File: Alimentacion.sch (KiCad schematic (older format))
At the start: 5 parts, among them CON1 BARREL_JACK, U4 LM7805CT

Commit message: finalizado enrutado provisional
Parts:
- D1: footprint Diodes_ThroughHole:Diode_DO-35_SOD27_Horizontal_RM10 -> Diodos:DO-214AC
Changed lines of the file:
@@
 $Descr A4 11693 8268
 encoding utf-8
-Sheet 3 14
+Sheet 2 15
 Title ""
 Date ""
@@
 F 0 "D1" H 4950 2700 50  0000 C CNN
 F 1 "1N4002" H 4950 2500 50  0000 C CNN
-F 2 "Diodes_ThroughHole:Diode_DO-35_SOD27_Horizontal_RM10" H 4950 2600 50  0001 C CNN
+F 2 "Diodos:DO-214AC" H 4950 2600 50  0001 C CNN
 F 3 "" H 4950 2600 50  0000 C CNN
 F 4 "DC COMPONENTS" H 4950 2600 60  0001 C CNN "Fabricante"
@@
 Alimentador de corriente\nTME AK-TB-02\nFabricante AKYGA\nRef: CPSUNOTAKY-07290
 $Comp
-L +5V #PWR08
+L +5V #PWR01
 U 1 1 5793C6D2
 P 7050 2450
-F 0 "#PWR08" H 7050 2300 50  0001 C CNN
+F 0 "#PWR01" H 7050 2300 50  0001 C CNN
 F 1 "+5V" H 7050 2590 50  0000 C CNN
 F 2 "" H 7050 2450 50  0000 C CNN
@@
 $EndComp
 $Comp
-L GND #PWR09
+L GND #PWR02
 U 1 1 5793C6D8
 P 6050 3350
-F 0 "#PWR09" H 6050 3100 50  0001 C CNN
+F 0 "#PWR02" H 6050 3100 50  0001 C CNN
 F 1 "GND" H 6050 3200 50  0000 C CNN
 F 2 "" H 6050 3350 50  0000 C CNN
@@
 $EndComp
 $Comp
-L PWR_FLAG #FLG010
+L PWR_FLAG #FLG03
 U 1 1 5793C6DE
 P 4650 2450
-F 0 "#FLG010" H 4650 2545 50  0001 C CNN
+F 0 "#FLG03" H 4650 2545 50  0001 C CNN
 F 1 "PWR_FLAG" H 4650 2630 50  0000 C CNN
 F 2 "" H 4650 2450 50  0000 C CNN
@@
 $EndComp
 $Comp
-L PWR_FLAG #FLG011
+L PWR_FLAG #FLG04
 U 1 1 5793C6E4
 P 4950 3100
-F 0 "#FLG011" H 4950 3195 50  0001 C CNN
+F 0 "#FLG04" H 4950 3195 50  0001 C CNN
 F 1 "PWR_FLAG" H 4950 3280 50  0000 C CNN
 F 2 "" H 4950 3100 50  0000 C CNN
@@
 $EndComp
 $Comp
-L VCC #PWR012
+L VCC #PWR05
 U 1 1 5793C6EA
 P 7300 2450
-F 0 "#PWR012" H 7300 2300 50  0001 C CNN
+F 0 "#PWR05" H 7300 2300 50  0001 C CNN
 F 1 "VCC" H 7300 2600 50  0000 C CNN
 F 2 "" H 7300 2450 50  0000 C CNN

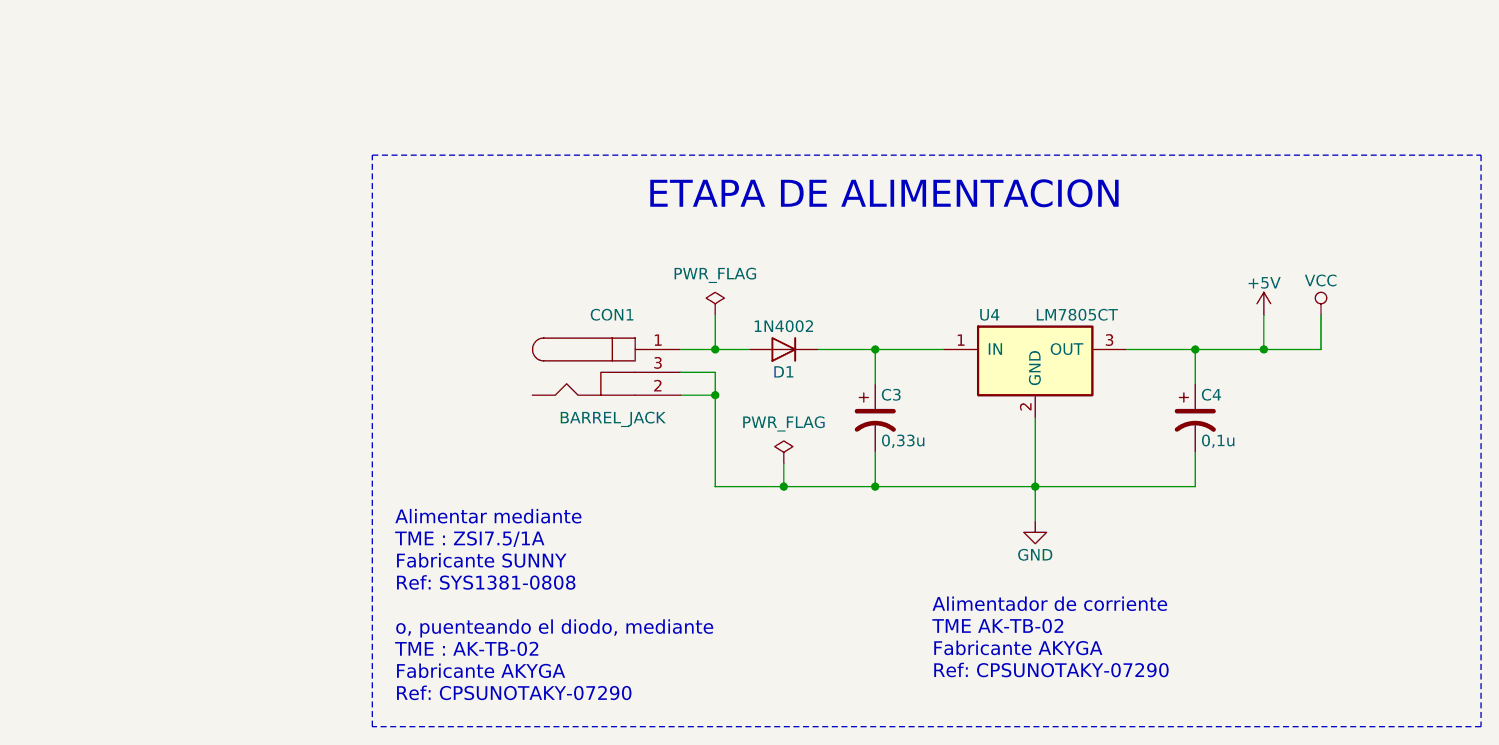
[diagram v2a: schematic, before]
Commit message: añadiendo valores del distribuidor a los componentes
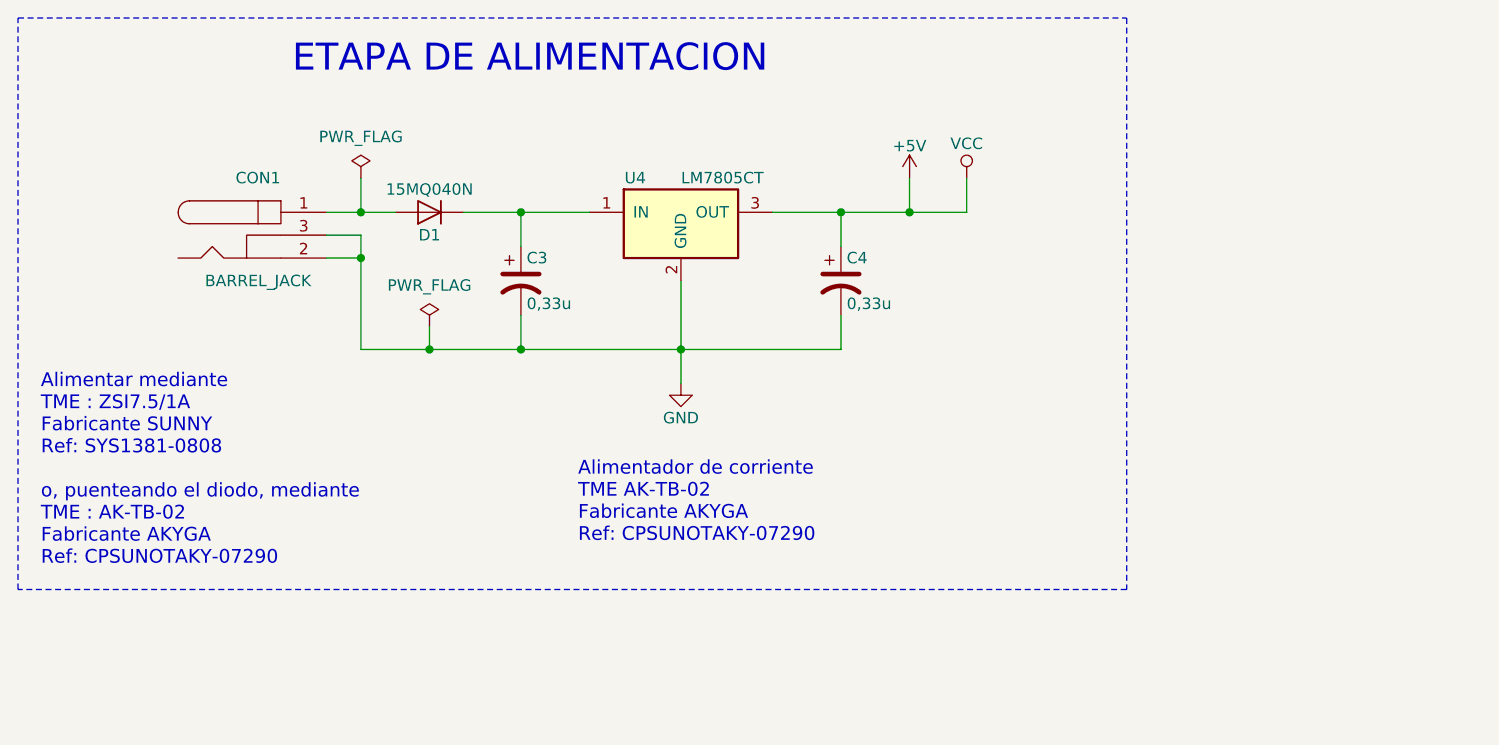
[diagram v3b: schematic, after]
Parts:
- C3: Ref UMT1HR33MDD -> UVZ1H330MDD; Ref_Proveedor UMT1HR33MDD -> UVZ1H330MDD
- C4: value 0,1u -> 0,33u; Ref UMT1H0R1MDD -> UVZ1H330MDD; Ref_Proveedor UMT1H0R1MDD -> UVZ1H330MDD
- D1: value 1N4002 -> 15MQ040N; Fabricante DC COMPONENTS -> VISHAY; Ref 1N4002 -> 15MQ040N; Ref_Proveedor 1N4002-DC -> 15MQ040NTRPBF
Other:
- moved on the sheet: C3, C4, CON1, D1, U4

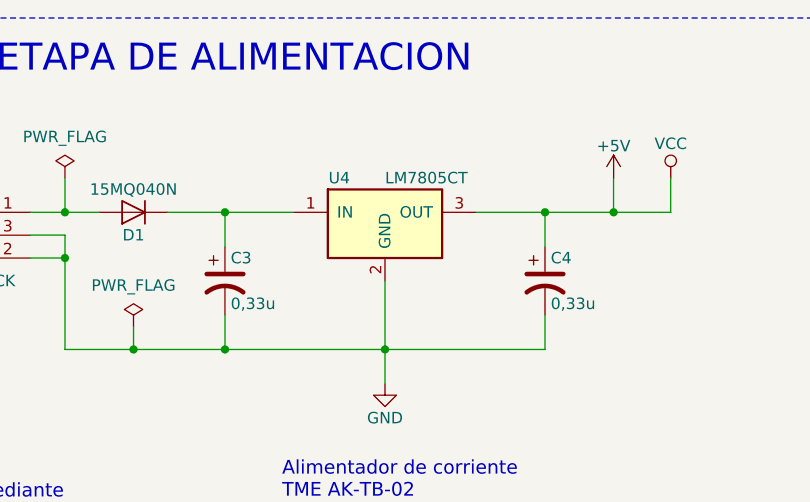
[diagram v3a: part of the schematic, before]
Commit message: ordenar referencias de componentes
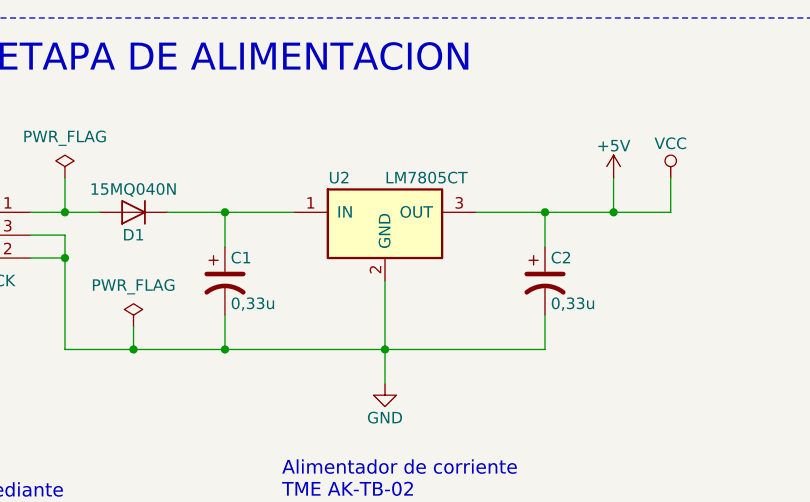
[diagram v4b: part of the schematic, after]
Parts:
- renumbered C3 to C1, C4 to C2, U4 to U2
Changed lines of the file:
@@
 $Descr User 8268 5846
 encoding utf-8
-Sheet 2 15
+Sheet 3 15
 Title ""
 Date ""
@@
 $EndComp
 $Comp
-L CP1 C3
+L CP1 C1
 U 1 1 5793C6BD
 P 3800 2300
-F 0 "C3" H 3825 2400 50  0000 L CNN
+F 0 "C1" H 3825 2400 50  0000 L CNN
 F 1 "0,33u" H 3825 2200 50  0000 L CNN
 F 2 "Capacitors_ThroughHole:C_Radial_D5_L11_P2" H 3800 2300 50  0001 C CNN
@@
 $EndComp
 $Comp
-L CP1 C4
+L CP1 C2
 U 1 1 5793C6CA
 P 5200 2300
-F 0 "C4" H 5225 2400 50  0000 L CNN
+F 0 "C2" H 5225 2400 50  0000 L CNN
 F 1 "0,33u" H 5225 2200 50  0000 L CNN
 F 2 "Capacitors_ThroughHole:C_Radial_D5_L11_P2" H 5200 2300 50  0001 C CNN
@@
 Alimentador de corriente\nTME AK-TB-02\nFabricante AKYGA\nRef: CPSUNOTAKY-07290
 $Comp
-L +5V #PWR01
+L +5V #PWR6
 U 1 1 5793C6D2
 P 5500 1850
-F 0 "#PWR01" H 5500 1700 50  0001 C CNN
+F 0 "#PWR6" H 5500 1700 50  0001 C CNN
 F 1 "+5V" H 5500 1990 50  0000 C CNN
 F 2 "" H 5500 1850 50  0000 C CNN
@@
 $EndComp
 $Comp
-L GND #PWR02
+L GND #PWR5
 U 1 1 5793C6D8
 P 4500 2750
-F 0 "#PWR02" H 4500 2500 50  0001 C CNN
+F 0 "#PWR5" H 4500 2500 50  0001 C CNN
 F 1 "GND" H 4500 2600 50  0000 C CNN
 F 2 "" H 4500 2750 50  0000 C CNN
@@
 $EndComp
 $Comp
-L PWR_FLAG #FLG03
+L PWR_FLAG #FLG1
 U 1 1 5793C6DE
 P 3100 1850
-F 0 "#FLG03" H 3100 1945 50  0001 C CNN
+F 0 "#FLG1" H 3100 1945 50  0001 C CNN
 F 1 "PWR_FLAG" H 3100 2030 50  0000 C CNN
 F 2 "" H 3100 1850 50  0000 C CNN
@@
 $EndComp
 $Comp
-L PWR_FLAG #FLG04
+L PWR_FLAG #FLG2
 U 1 1 5793C6E4
 P 3400 2500
-F 0 "#FLG04" H 3400 2595 50  0001 C CNN
+F 0 "#FLG2" H 3400 2595 50  0001 C CNN
 F 1 "PWR_FLAG" H 3400 2680 50  0000 C CNN
 F 2 "" H 3400 2500 50  0000 C CNN
@@
 $EndComp
 $Comp
-L VCC #PWR05
+L VCC #PWR7
 U 1 1 5793C6EA
 P 5750 1850
-F 0 "#PWR05" H 5750 1700 50  0001 C CNN
+F 0 "#PWR7" H 5750 1700 50  0001 C CNN
 F 1 "VCC" H 5750 2000 50  0000 C CNN
 F 2 "" H 5750 1850 50  0000 C CNN
@@
 	3550 2000 4100 2000
 $Comp
-L LM7805CT U4
+L LM7805CT U2
 U 1 1 5793C70E
 P 4500 2050
-F 0 "U4" H 4300 2250 50  0000 C CNN
+F 0 "U2" H 4300 2250 50  0000 C CNN
 F 1 "LM7805CT" H 4500 2250 50  0000 L CNN
 F 2 "TO_SOT_Packages_THT:TO-220_Neutral123_Vertical_LargePads" H 4500 2150 50  0001 C CIN

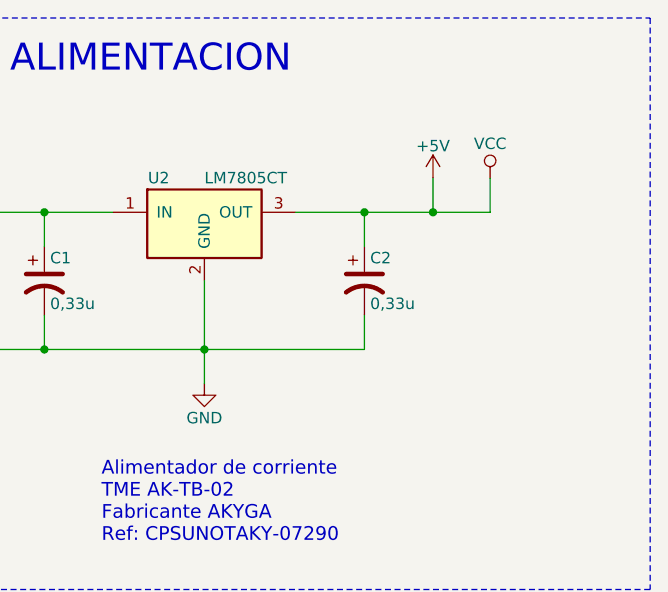
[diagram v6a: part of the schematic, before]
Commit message: añadidos driver para led y conectores para fotodiodos infrarrojos
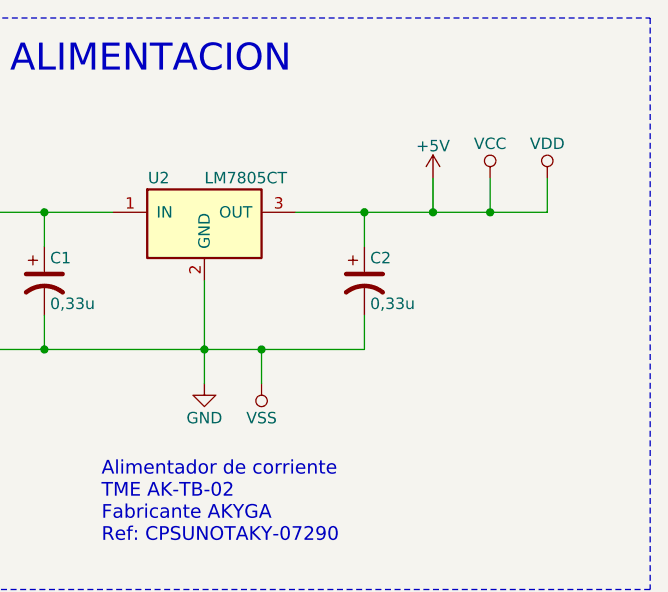
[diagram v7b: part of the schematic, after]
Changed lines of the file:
@@
 EESchema Schematic File Version 2
+LIBS:Interfaces
+LIBS:Nano_PB-rescue
 LIBS:Sensores
 LIBS:power
@@
 LIBS:valves
 LIBS:MyLibrary
+LIBS:matriz_led
 LIBS:Nano_PB-cache
-EELAYER 25 0
+EELAYER 26 0
 EELAYER END
 $Descr User 8268 5846
 encoding utf-8
-Sheet 3 15
+Sheet 3 16
 Title "Etapa de alimentación"
-Date "2016-08-07"
-Rev "V.0.2"
+Date "2017-01-04"
+Rev "V.0.3"
 Comp "NanoPlayBoard"
 Comment1 "Creada por Antonio Morales"
@@
 Wire Wire Line
 	5200 2150 5200 2000
-Wire Wire Line
-	4900 2000 5750 2000
 Connection ~ 4500 2600
 Wire Wire Line
@@
 50 17 92 01 51 92 64 0C CE 27 7B 4E 87 A3 FC C9 E9 39 BC D0 3B DC 1F CF E6 3C 60 30 83 10 3D 18
 F4 0B 89 52 73 00 8B 80 91 08 28 22 8F 6D AB AA BD D3 E7 C4 3E A7 59 B4 A9 94 4D 1C A1 84 52 AC
-9A 46 F6 7A E1 FF 00 F0 A4 0C 74 26 CB 7B D1 00 00 00 00 49 45 4E 44 AE 42 60 82 00
+9A 46 F6 7A E1 FF 00 F0 A4 0C 74 26 CB 7B D1 00 00 00 00 49 45 4E 44 AE 42 60 82
 EndData
 $EndBitmap
+Wire Wire Line
+	4900 2000 6000 2000
+$Comp
+L VSS #PWR010
+U 1 1 587197E0
+P 4750 2750
+F 0 "#PWR010" H 4750 2600 50  0001 C CNN
+F 1 "VSS" H 4750 2900 50  0000 C CNN
+F 2 "" H 4750 2750 50  0000 C CNN
+F 3 "" H 4750 2750 50  0000 C CNN
+	1    4750 2750
+	-1   0    0    1
+$EndComp
+Wire Wire Line
+	4750 2750 4750 2600
+Connection ~ 4750 2600
+$Comp
+L VDD #PWR011
+U 1 1 58719840
+P 6000 1850
+F 0 "#PWR011" H 6000 1700 50  0001 C CNN
+F 1 "VDD" H 6000 2000 50  0000 C CNN
+F 2 "" H 6000 1850 50  0000 C CNN
+F 3 "" H 6000 1850 50  0000 C CNN
+	1    6000 1850
+	1    0    0    -1
+$EndComp
+Wire Wire Line
+	6000 2000 6000 1850
+Connection ~ 5750 2000
 $EndSCHEMATC
